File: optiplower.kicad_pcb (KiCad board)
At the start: 2 copper layers, 71.9 x 17.2 mm, 22 parts, among them J1 Conn_01x02, J2 Conn_01x03, U1 LR7533-M, U2 XL4015, U3 DS2502, U4 ATtiny25-20SS, U5 ATtiny85-20P, U6 DS2502S+

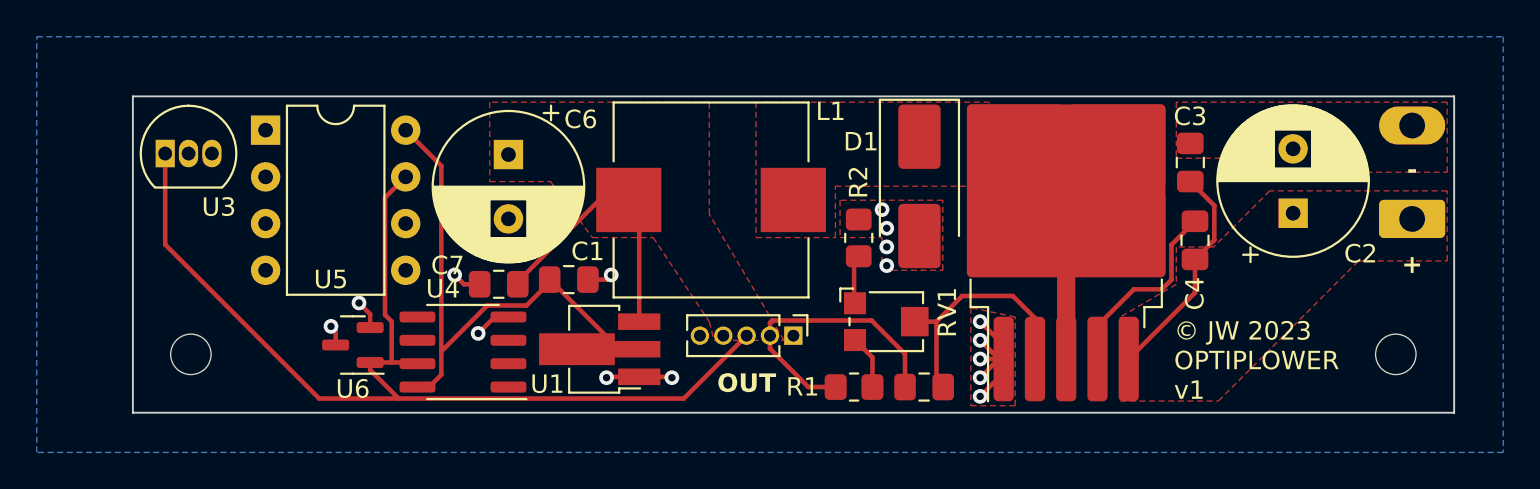
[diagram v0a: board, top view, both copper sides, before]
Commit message: Fix 3.3v regulator pinout
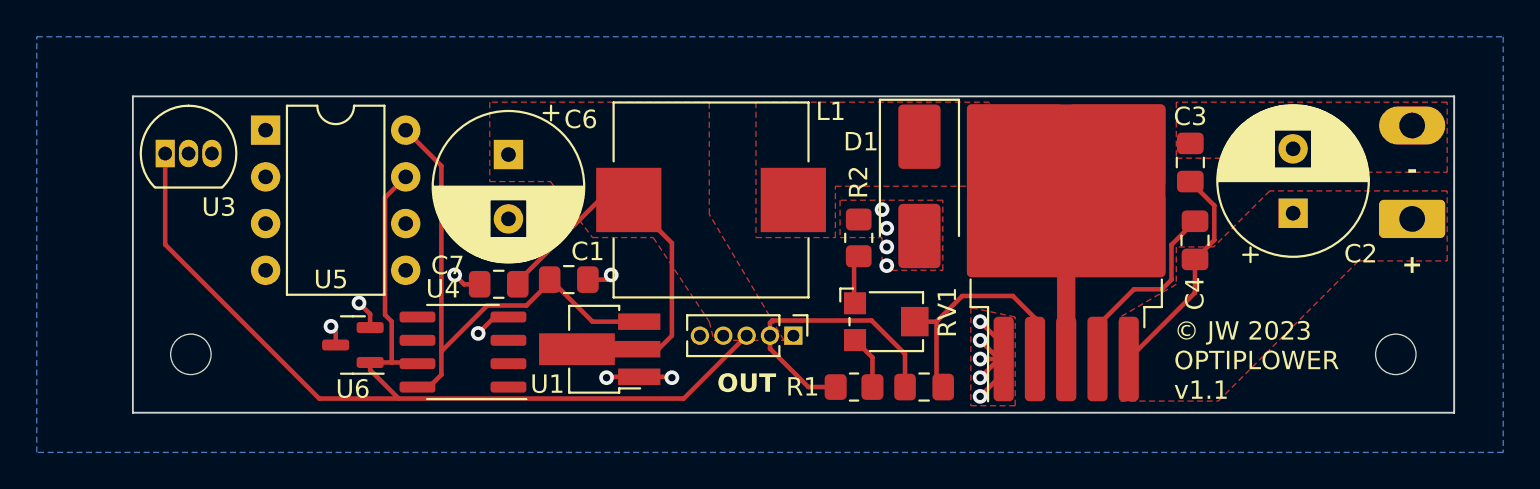
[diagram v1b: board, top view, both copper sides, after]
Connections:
- U1 pad 2: +3V3 -> VCC
- U1 pad 3: VCC -> +3V3
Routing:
- net VCC: track 30.7 -> 35.3 mm
- net +3V3: track 29.6 -> 29.1 mm
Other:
- board text added: "© JW 2023 OPTIPLOWER v1.1"
- board text removed: "© JW 2023 OPTIPLOWER v1"
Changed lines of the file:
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@@
       (net 2 "GND") (pinfunction "GND") (pintype "power_in"))
     (pad "2" smd custom (at -2.3625 0 180) (size 2.475 0.9) (layers "F.Cu" "F.Paste" "F.Mask")
-      (net 1 "+3V3") (pinfunction "VO") (pintype "power_out") (zone_connect 2) (thermal_bridge_angle 45)
+      (net 5 "VCC") (pinfunction "VI") (pintype "power_in") (zone_connect 2) (thermal_bridge_angle 45)
       (options (clearance outline) (anchor rect))
       (primitives
@@
       ))
     (pad "3" smd rect (at -2.45 1.5 180) (size 2.3 0.9) (layers "F.Cu" "F.Paste" "F.Mask")
-      (net 5 "VCC") (pinfunction "VI") (pintype "power_in"))
+      (net 1 "+3V3") (pinfunction "VO") (pintype "power_out"))
     (model "${KICAD6_3DMODEL_DIR}/Package_TO_SOT_SMD.3dshapes/SOT-89-3.wrl"
       (offset (xyz 0 0 0))
@@
     (effects (font (size 1 1) (thickness 0.2) bold) (justify bottom))
   )
-  (gr_text "© JW 2023\nOPTIPLOWER\nv1" (at 241.681 94.996) (layer "F.SilkS")
+  (gr_text "© JW 2023\nOPTIPLOWER\nv1.1" (at 241.681 94.996) (layer "F.SilkS")
     (effects (font (size 1 1) (thickness 0.15)) (justify left bottom))
   )
@@
     (effects (font (size 1 1) (thickness 0.2) bold))
   )
+  (segment (start 212.598 90.678) (end 210.058 90.678) (width 0.25) (layer "F.Cu") (net 1))
   (segment (start 204.333 89.799) (end 201.836 92.296) (width 0.25) (layer "F.Cu") (net 1))
   (segment (start 207.729 88.392) (end 207.729 88.536673) (width 0.25) (layer "F.Cu") (net 1))
   (segment (start 201.168 94.234) (end 200.536 94.234) (width 0.25) (layer "F.Cu") (net 1))
   (segment (start 201.836 92.296) (end 201.836 93.566) (width 0.25) (layer "F.Cu") (net 1))
+  (segment (start 210.058 90.678) (end 207.772 88.392) (width 0.25) (layer "F.Cu") (net 1))
   (segment (start 199.898 80.264) (end 201.836 82.202) (width 0.25) (layer "F.Cu") (net 1))
-  (segment (start 211.515 92.178) (end 212.5105 92.178) (width 0.25) (layer "F.Cu") (net 1))
+  (segment (start 207.772 88.392) (end 207.729 88.392) (width 0.25) (layer "F.Cu") (net 1))
   (segment (start 201.836 93.566) (end 201.168 94.234) (width 0.25) (layer "F.Cu") (net 1))
   (segment (start 206.466673 89.799) (end 204.333 89.799) (width 0.25) (layer "F.Cu") (net 1))
-  (segment (start 207.729 88.392) (end 211.515 92.178) (width 0.25) (layer "F.Cu") (net 1))
   (segment (start 207.729 88.536673) (end 206.466673 89.799) (width 0.25) (layer "F.Cu") (net 1))
   (segment (start 201.836 82.202) (end 201.836 92.296) (width 0.25) (layer "F.Cu") (net 1))
@@
   (segment (start 210.435327 84.06) (end 212.03 84.06) (width 0.25) (layer "F.Cu") (net 5))
   (segment (start 225.235 90.615) (end 219.827894 90.615) (width 0.25) (layer "F.Cu") (net 5))
+  (segment (start 214.376 91.44) (end 214.376 86.406) (width 0.25) (layer "F.Cu") (net 5))
+  (segment (start 213.638 92.178) (end 214.376 91.44) (width 0.25) (layer "F.Cu") (net 5))
   (segment (start 219.71 90.732894) (end 219.71 91.44) (width 0.25) (layer "F.Cu") (net 5))
   (segment (start 227.0545 94.234) (end 227.0545 92.4345) (width 0.25) (layer "F.Cu") (net 5))
   (segment (start 223.282 94.234) (end 221.796894 94.234) (width 0.25) (layer "F.Cu") (net 5))
+  (segment (start 214.376 86.406) (end 212.03 84.06) (width 0.25) (layer "F.Cu") (net 5))
+  (segment (start 211.515 92.178) (end 212.5105 92.178) (width 0.25) (layer "F.Cu") (net 5))
   (segment (start 227.0545 92.4345) (end 225.235 90.615) (width 0.25) (layer "F.Cu") (net 5))
-  (segment (start 212.598 84.628) (end 212.03 84.06) (width 0.25) (layer "F.Cu") (net 5))
-  (segment (start 212.598 90.678) (end 212.598 84.628) (width 0.25) (layer "F.Cu") (net 5))
+  (segment (start 212.5105 92.178) (end 213.638 92.178) (width 0.25) (layer "F.Cu") (net 5))
   (segment (start 205.994 88.501327) (end 210.435327 84.06) (width 0.25) (layer "F.Cu") (net 5))
   (segment (start 219.827894 90.615) (end 219.71 90.732894) (width 0.25) (layer "F.Cu") (net 5))
